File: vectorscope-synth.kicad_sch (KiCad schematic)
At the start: 22 parts, among them J1 STYLUS, J2 IO CONNECTOR, J3 SCOPE, J4 SIGGEN, J5 PATCH SELECT, J6 WRITE PATCH, J7 PARAM SELECT, J8 MODE, SW1 SW_SPST, SW2 SW_SPST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

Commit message: Credits, and schematic PDF
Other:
- moved on the sheet: AMP1, C1, C2, J2, J3, J4, LS1, R1, R2, R3, RGB1, SW1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

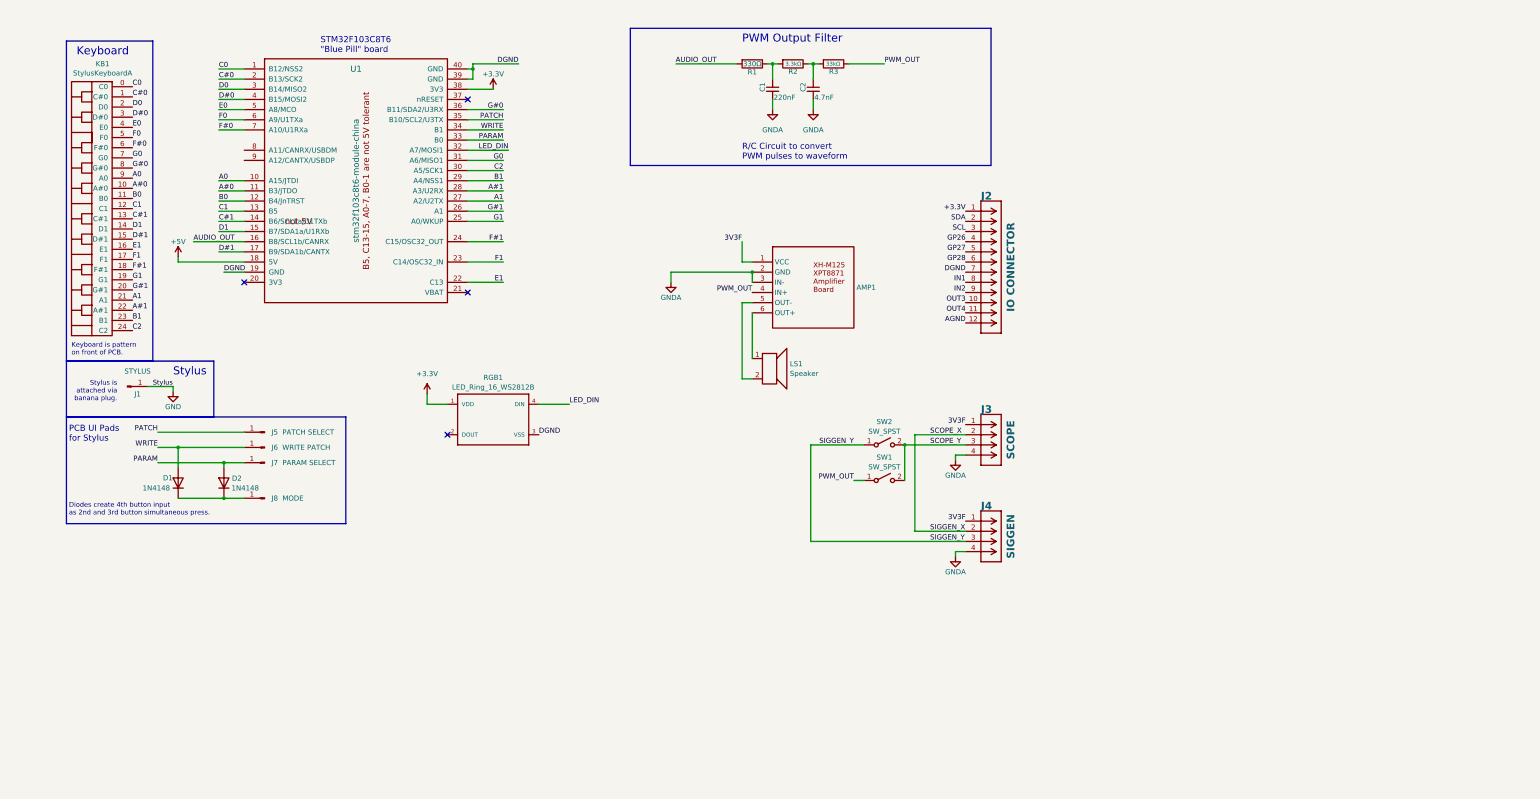
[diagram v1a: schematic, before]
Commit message: Added op amp LM358 circuit to move PWM levels to vectorscope 0-3.3v. Replaced XH-M125/XPT8871 amp with GF1002/PAM8403 stereo amp with volume control. Enlarged many traces. Added logos for SoftEgg and Aisler. Learned that none of our passives or opamps had been ordered. Learned that our supplier only has 9 LED rings. Continued panicing...
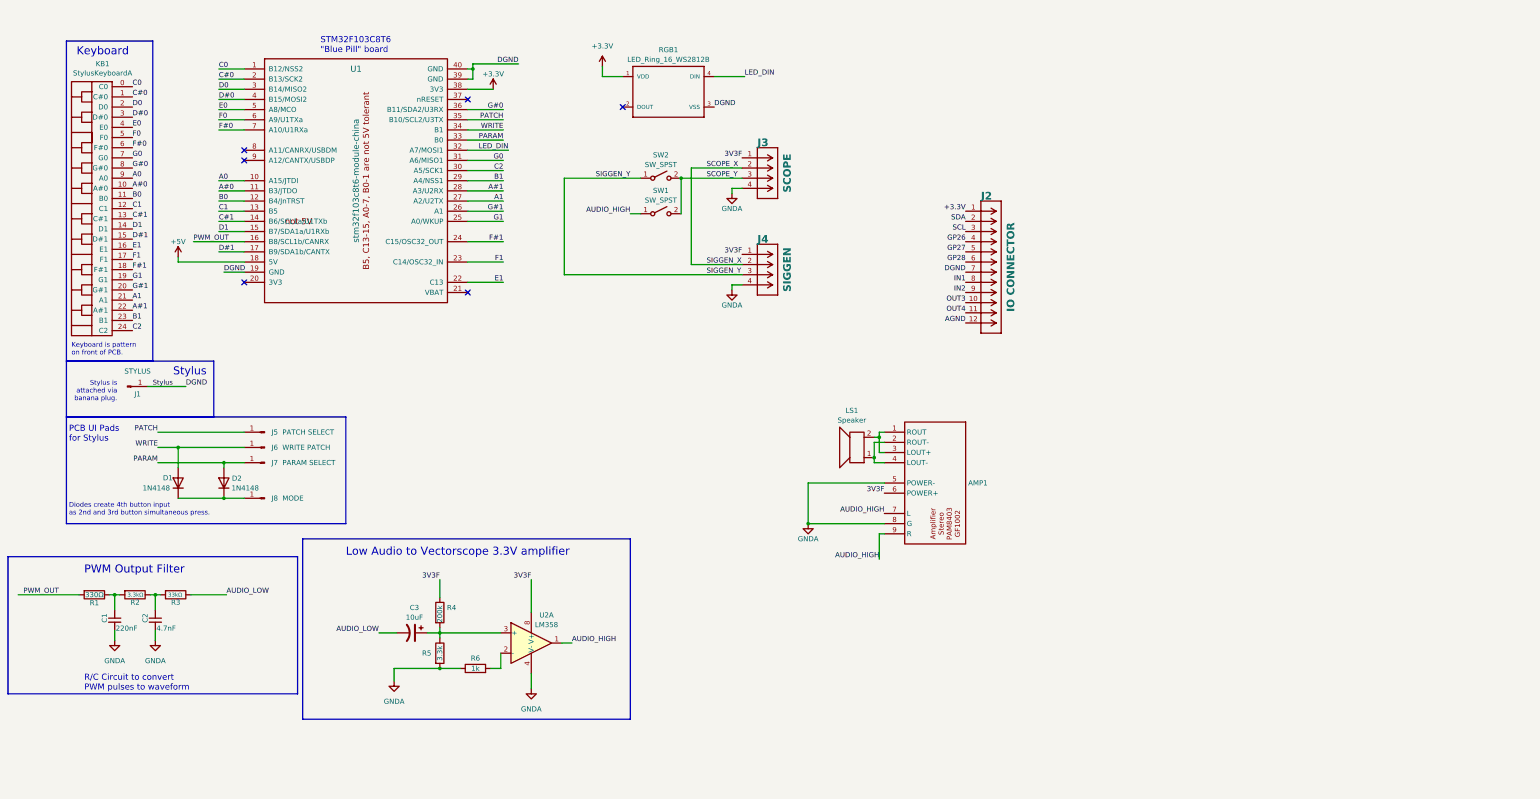
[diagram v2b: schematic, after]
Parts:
- removed AMP1: ~, SoftEggKiCAD:XH-M125 Amplifier Board, symbol SoftEgg:XH-M125_Amplifier_Board
- added AMP1: ~, SoftEggKiCAD:GF1002-PAM8403_Amplifier_Module, symbol SoftEgg:GF1002-PAM8403_Amplifier_Module
- added C3: 10uF, Capacitor_THT:CP_Radial_D5.0mm_P2.50mm, symbol .vector:CAP_POL
- added R4: 200k, SoftEggKiCAD:R_Axial_DIN0204_L3.6mm_D1.6mm_P5mm_Horizontal+SMD804, symbol Device:R
- added R5: 3.3k, SoftEggKiCAD:R_Axial_DIN0204_L3.6mm_D1.6mm_P5mm_Horizontal+SMD804, symbol Device:R
- added R6: 1k, SoftEggKiCAD:R_Axial_DIN0204_L3.6mm_D1.6mm_P5mm_Horizontal+SMD804, symbol Device:R
- added U2: LM358, Package_DIP:DIP-8_W7.62mm_LongPads, symbol Amplifier_Operational:LM358
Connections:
- net AUDIO_OUT is gone; now on net PWM_OUT: R1.2, U1.16 (B8/SCL1b/CANRX)
- net GND is gone; now on net DGND: J1.1 (Pin_1)
- net 3V3F: now also AMP1.6 (POWER+), R4.1, U2.8 (V+)
- net GNDA: now also AMP1.5 (POWER-), AMP1.8 (G), R5.2, R6.1, U2.4 (V-)
- net PWM_OUT: no longer R3.1, SW1.1 (A)
- net at LS1.1: now also AMP1.2 (ROUT-), AMP1.4 (LOUT-)
- net at LS1.2: now also AMP1.1 (ROUT), AMP1.3 (LOUT+)
- new net: C3.1, R4.2, R5.1, U2.3 (+)
- new net: R6.2, U2.2 (-)
- new net AUDIO_HIGH: AMP1.7 (L), AMP1.9 (R), SW1.1 (A), U2.1
- new net AUDIO_LOW: C3.2, R3.1
- no-connect marks 4 -> 6
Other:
- note added: "Low Audio to Vectorscope 3.3V amplifier"
- moved on the sheet: C1, C2, J3, J4, R1, R2, R3, RGB1, SW1, SW2

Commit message: PCB and Schematic updates by Thea @ Aisler
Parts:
- removed SW1, SW2: SW_SPST, Connector_PinHeader_2.54mm:PinHeader_1x03_P2.54mm_Vertical, symbol .vector:SW_SPST
- added J9: Conn_01x02_Pin, Connector_PinHeader_2.54mm:PinHeader_1x02_P2.54mm_Vertical, symbol Connector:Conn_01x02_Pin
- added NT1: NetTie_3, NetTie:NetTie-3_SMD_Pad0.5mm, symbol Device:NetTie_3
- added R7, R8: 200k, Diode+THT+SMD:R_Axial_DIN0204_L3.6mm_D1.6mm_P7.62mm_Horizontal+SMD804, symbol Device:R
- added SW3, SW4: SW_SPDT, Connector_PinHeader_2.54mm:PinHeader_1x03_P2.54mm_Vertical, symbol Switch:SW_SPDT
- added unit 3 of U2
- added unit 2 of U2
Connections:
- net +3.3V: now also AMP1.6 (POWER+), R4.1, SW3.2 (B), U2.8 (V+); no longer J2.1
- net AUDIO_HIGH: now also SW4.3 (C); no longer AMP1.7 (L)
- net DGND: now also NT1.1; no longer J2.7
- net GNDA: now also NT1.3, R7.1, R8.1, U2.4 (V-); no longer U2.4 (V-)
- net SCOPE_Y: now also SW4.2 (B)
- net SIGGEN_Y: now also SW4.1 (A)
- net at AMP1.1 (ROUT), LS1.2: no longer AMP1.3 (LOUT+)
- net at AMP1.2 (ROUT-), LS1.1: no longer AMP1.4 (LOUT-)
- net +5V: no longer names the net of U1.18 (5V)
- removed net 3V3F: AMP1.6 (POWER+), J3.1 (Pin_1), J4.1 (Pin_1), R4.1, U2.8 (V+)
- new net: R7.2, U2.5 (+)
- new net: AMP1.7 (L), R8.2
- new net: J9.1 (Pin_1), SW3.3 (C)
- new net: U2.6 (-), U2.7
- new net +3.3V-IN: J2.1, SW3.1 (A)
- new net GND-IN: J2.7, J9.2 (Pin_2), NT1.2
- no-connect marks 6 -> 11
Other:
- moved on the sheet: LS1

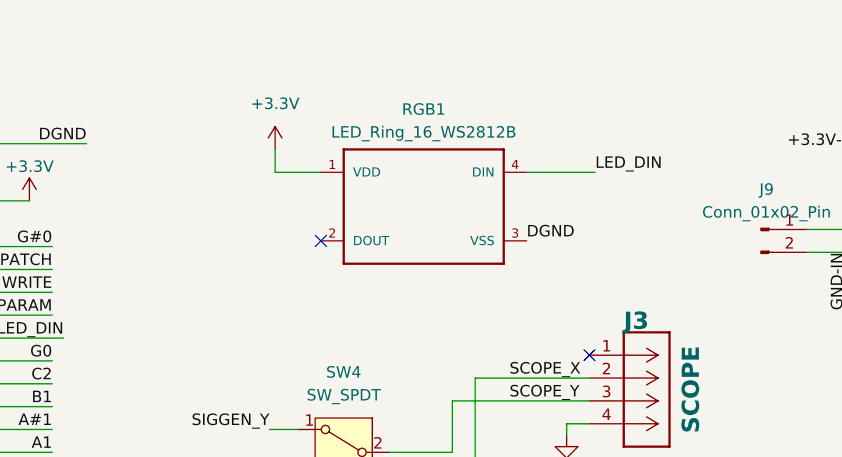
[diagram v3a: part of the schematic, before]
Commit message: Note: This is NOT the version used in the Hackaday Europe 2024 Workshop, that is the previous version. This is a version that fixes the LED ring wiring problem with that one, and has a footprint that more correctly shows the size of that LED ring. There may still be other issues... I'll find out when I go to build one from that PCB tomorrow.
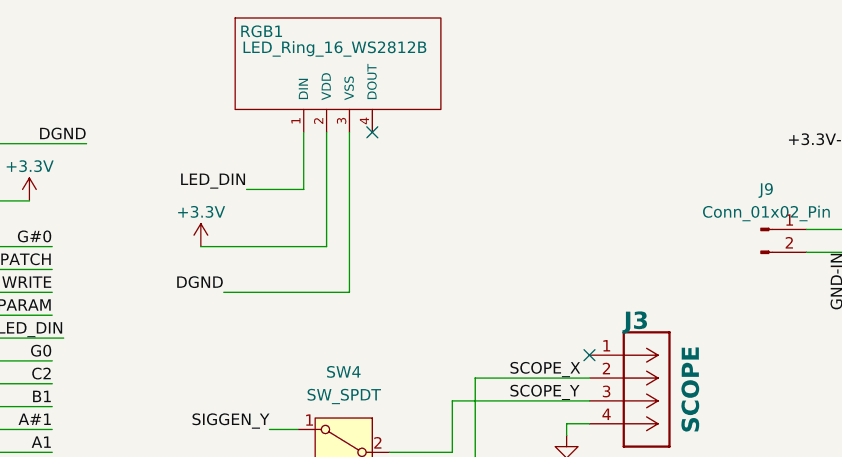
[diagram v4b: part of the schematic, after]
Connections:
- net +3.3V: now also RGB1.2 (VDD); no longer RGB1.1 (VDD)
- net LED_DIN: now also RGB1.1 (DIN); no longer RGB1.4 (DIN)
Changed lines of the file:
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@@
 	)
 	(no_connect
-		(at 173.355 42.545)
+		(at 179.07 30.48)
 	)
 	(no_connect
@@
 		)
 	)
+	(wire
+		(pts
+			(xy 176.53 48.26) (xy 176.53 30.48)
+		)
+		(stroke
+			(width 0)
+			(type default)
+		)
+	)
 	(polyline
 		(pts
@@
 	(wire
 		(pts
-			(xy 173.355 34.925) (xy 168.275 34.925)
+			(xy 156.845 129.54) (xy 160.02 129.54)
 		)
 		(stroke
@@
 	(wire
 		(pts
-			(xy 156.845 129.54) (xy 160.02 129.54)
+			(xy 246.38 46.99) (xy 242.57 46.99)
 		)
 		(stroke
@@
 	(wire
 		(pts
-			(xy 246.38 46.99) (xy 242.57 46.99)
+			(xy 134.62 63.5) (xy 143.51 63.5)
 		)
 		(stroke
@@
 	(wire
 		(pts
-			(xy 134.62 63.5) (xy 143.51 63.5)
+			(xy 22.225 164.465) (xy 37.465 164.465)
 		)
 		(stroke
@@
 	(wire
 		(pts
-			(xy 22.225 164.465) (xy 37.465 164.465)
+			(xy 233.045 32.385) (xy 236.855 32.385)
 		)
 		(stroke
@@
 	(wire
 		(pts
-			(xy 233.045 32.385) (xy 236.855 32.385)
+			(xy 173.99 43.18) (xy 173.99 30.48)
 		)
 		(stroke
@@
 	(wire
 		(pts
-			(xy 196.215 34.925) (xy 203.835 34.925)
-		)
-		(stroke
-			(width 0)
-			(type default)
-		)
-	)
-	(wire
-		(pts
 			(xy 245.11 52.07) (xy 245.11 49.53)
 		)
@@
 	(wire
 		(pts
+			(xy 165.1 36.83) (xy 171.45 36.83)
+		)
+		(stroke
+			(width 0)
+			(type default)
+		)
+	)
+	(wire
+		(pts
 			(xy 236.22 139.065) (xy 238.76 139.065)
 		)
@@
 	(wire
 		(pts
-			(xy 168.275 34.925) (xy 168.275 32.385)
-		)
-		(stroke
-			(width 0)
-			(type default)
-		)
-	)
-	(wire
-		(pts
 			(xy 46.355 164.465) (xy 47.625 164.465)
 		)
@@
 	(wire
 		(pts
+			(xy 162.56 48.26) (xy 176.53 48.26)
+		)
+		(stroke
+			(width 0)
+			(type default)
+		)
+	)
+	(wire
+		(pts
 			(xy 56.515 164.465) (xy 57.785 164.465)
 		)
@@
 	(wire
 		(pts
+			(xy 160.02 43.18) (xy 173.99 43.18)
+		)
+		(stroke
+			(width 0)
+			(type default)
+		)
+	)
+	(wire
+		(pts
 			(xy 127.635 173.99) (xy 127.635 175.26)
 		)
@@
 	(wire
 		(pts
+			(xy 171.45 36.83) (xy 171.45 30.48)
+		)
+		(stroke
+			(width 0)
+			(type default)
+		)
+	)
+	(wire
+		(pts
 			(xy 230.505 123.825) (xy 238.76 123.825)
 		)
@@
 	)
 	(label "DGND"
-		(at 196.215 42.545 0)
+		(at 162.56 48.26 180)
 		(fields_autoplaced yes)
 		(effects
@@
 				(size 1.27 1.27)
 			)
-			(justify left bottom)
+			(justify right bottom)
 		)
 	)
@@
 	)
 	(label "LED_DIN"
-		(at 203.835 34.925 0)
+		(at 165.1 36.83 180)
 		(fields_autoplaced yes)
 		(effects
@@
 				(size 1.27 1.27)
 			)
-			(justify left bottom)
+			(justify right bottom)
 		)
 	)
@@
 	(symbol
 		(lib_id "power:+3.3V")
-		(at 168.275 32.385 0)
+		(at 160.02 43.18 0)
 		(mirror y)
 		(unit 1)
@@
 		(on_board yes)
 		(dnp no)
-		(fields_autoplaced yes)
 		(property "Reference" "#PWR05"
-			(at 168.275 36.195 0)
+			(at 160.02 46.99 0)
 			(effects
 				(font
@@
 		)
 		(property "Value" "+3.3V"
-			(at 168.275 27.305 0)
+			(at 160.02 39.37 0)
 			(effects
 				(font
@@
 		)
 		(property "Footprint" ""
-			(at 168.275 32.385 0)
+			(at 160.02 43.18 0)
 			(effects
 				(font
@@
 		)
 		(property "Datasheet" ""
-			(at 168.275 32.385 0)
+			(at 160.02 43.18 0)
 			(effects
 				(font
@@
 		)
 		(property "Description" ""
-			(at 168.275 32.385 0)
+			(at 160.02 43.18 0)
 			(effects
 				(font
@@
 	(symbol
 		(lib_id "SoftEgg:LED_Ring_16_WS2812B")
-		(at 178.435 40.005 0)
+		(at 171.45 30.48 0)
 		(unit 1)
 		(exclude_from_sim no)
@@
 		(on_board yes)
 		(dnp no)
-		(fields_autoplaced yes)
 		(property "Reference" "RGB1"
-			(at 184.785 27.94 0)
+			(at 164.338 19.304 0)
 			(effects
 				(font
 					(size 1.27 1.27)
 				)
+				(justify left)
 			)
 		)
 		(property "Value" "LED_Ring_16_WS2812B"
-			(at 184.785 30.48 0)
+			(at 164.592 21.082 0)
 			(effects
 				(font
 					(size 1.27 1.27)
 				)
+				(justify left)
 			)
 		)
 		(property "Footprint" "SoftEggKiCAD:LED RING 16 WS2812B"
-			(at 175.895 49.911 0)
+			(at 168.91 40.386 0)
 			(effects
 				(font
@@
 		)
 		(property "Datasheet" "None"
-			(at 175.895 51.943 0)
+			(at 168.91 42.418 0)
 			(effects
 				(font
@@
 		)
 		(property "Description" ""
-			(at 178.435 40.005 0)
+			(at 171.45 30.48 0)
 			(effects
 				(font

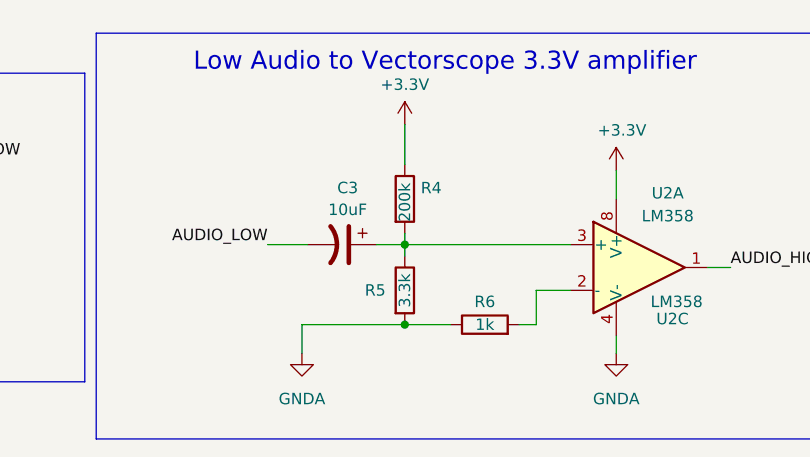
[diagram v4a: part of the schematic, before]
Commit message: Changed Resstor to give good values for the vector scope. Updated headers to give proper credits.
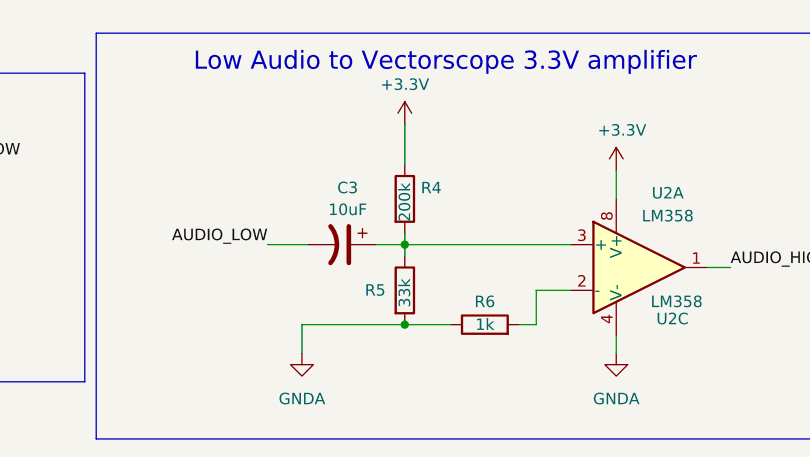
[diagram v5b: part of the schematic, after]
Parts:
- R5: value 3.3k -> 33k
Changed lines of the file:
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@@
 	(title_block
 		(title "Vectorscope Synthesizer")
-		(date "2024-04-08")
-		(rev "0.3")
+		(date "2024-04-11")
+		(rev "0.4")
 		(company "SoftEgg")
-		(comment 1 "Version 0.2 - T.B. Trzepacz @ SoftEgg  7.4.2024")
-		(comment 2 "Version 0.3 - Thea @ Aisler")
+		(comment 1 "Version 0.2 - T.B. Trzepacz @ SoftEgg  2024-4-7")
+		(comment 2 "Version 0.3 - Thea @ Aisler 2024-4-8")
+		(comment 3 "Version 0.4 - T. B. Trzepacz @ SoftEgg 2024-4-11")
 	)
 	(junction
@@
 			)
 		)
-		(property "Value" "3.3k"
+		(property "Value" "33k"
 			(at 127.635 180.975 90)
 			(effects

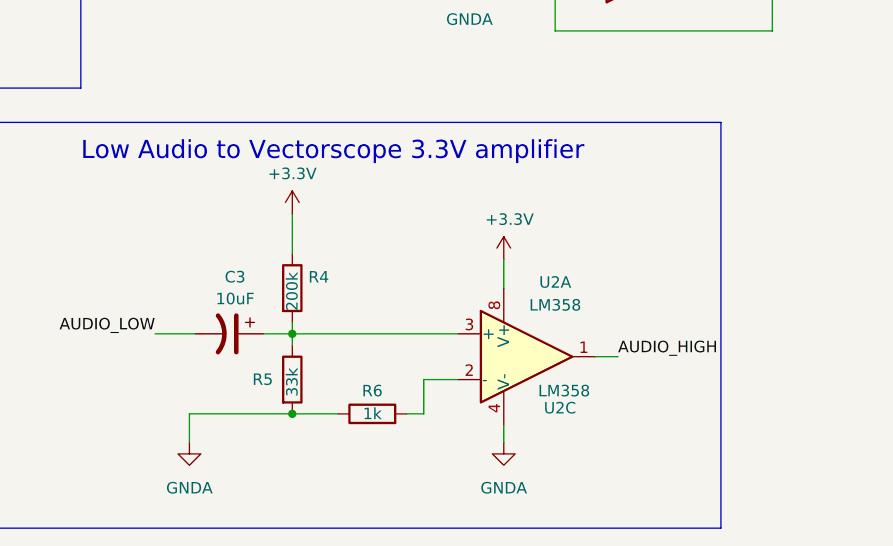
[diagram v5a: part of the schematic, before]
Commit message: propsed solution to amp problem
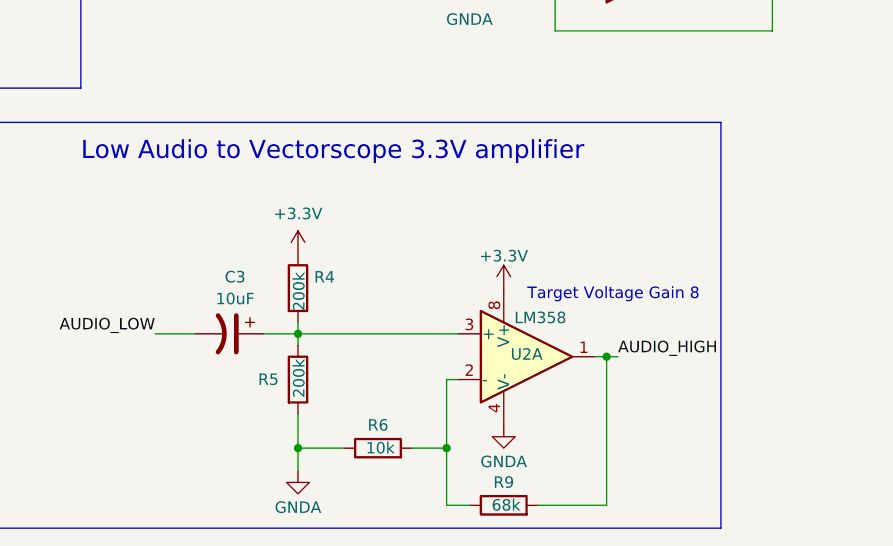
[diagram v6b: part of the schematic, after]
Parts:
- added R9: 68k, SoftEggKiCAD:R_Axial_DIN0204_L3.6mm_D1.6mm_P5mm_Horizontal+SMD804, symbol Device:R
- R5: value 33k -> 200k
- R6: value 1k -> 10k
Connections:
- net AUDIO_HIGH: now also R9.2
- net at R6.2, U2.2 (-): now also R9.1
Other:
- note added: "Target Voltage Gain 8"
- moved on the sheet: R4, R5, R6

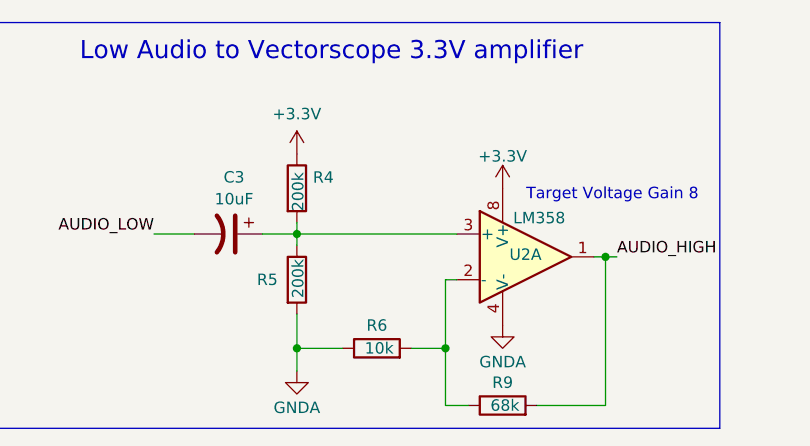
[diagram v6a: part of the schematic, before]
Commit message: correct patch resistor values for updated measurements
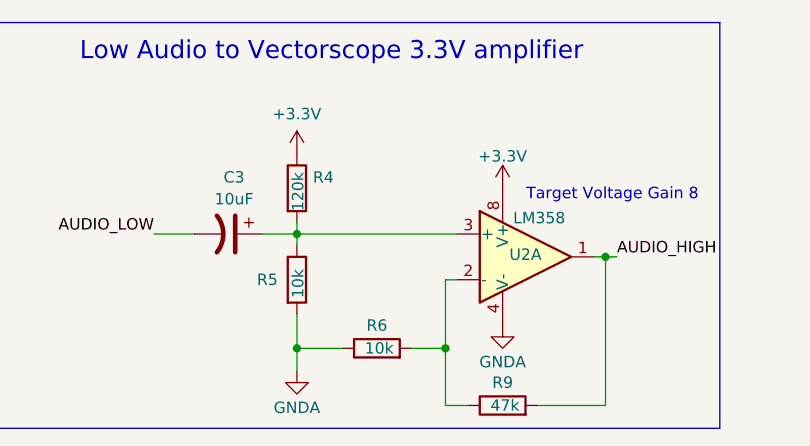
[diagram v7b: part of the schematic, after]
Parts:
- R4: value 200k -> 120k
- R5: value 200k -> 10k
- R9: value 68k -> 47k
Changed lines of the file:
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@@
 			)
 		)
-		(property "Value" "200k"
+		(property "Value" "10k"
 			(at 128.397 181.102 90)
 			(effects
@@
 			)
 		)
-		(property "Value" "68k"
+		(property "Value" "47k"
 			(at 151.384 193.04 90)
 			(effects
@@
 			)
 		)
-		(property "Value" "200k"
+		(property "Value" "120k"
 			(at 128.397 171.45 90)
 			(effects
